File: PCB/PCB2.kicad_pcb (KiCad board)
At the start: 2 copper layers, 19.2 x 13.5 mm, 8 parts, among them J1 USB_C_Receptacle_PowerOnly_6P, Q1 T2N7002AK

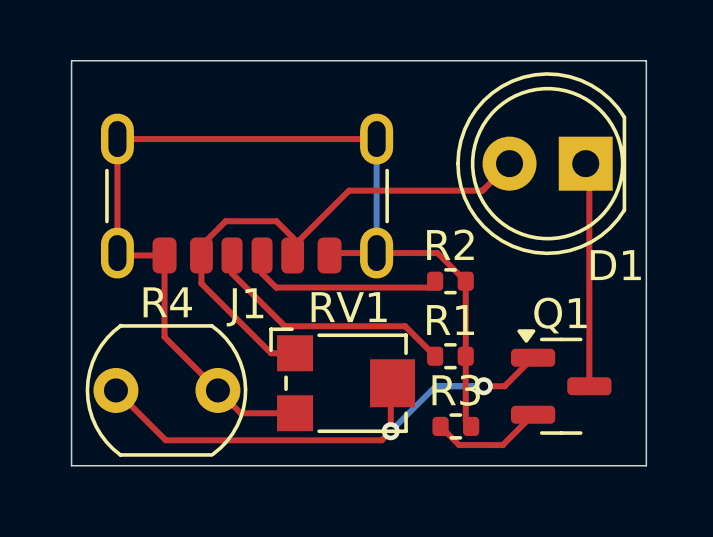
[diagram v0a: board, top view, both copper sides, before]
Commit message: Move LED to back of PCB
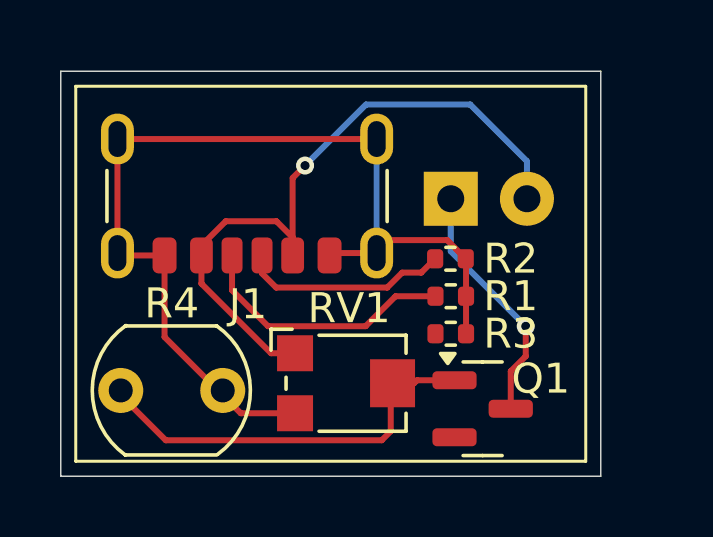
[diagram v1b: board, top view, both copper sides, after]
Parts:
- D1: moved to B.Cu
- moved D1 4.65 mm to (154.5, 93.2), turned to 0 degrees
- moved R3 3.09 mm to (154.5, 97.8)
- moved Q1 2.73 mm to (155.6, 100.2)
- moved R1 2.00 mm to (154.5, 96.5)
- moved R2 0.75 mm to (154.5, 95.2)
- moved R4 0.16 mm to (143.5, 99.6)
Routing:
- net Net-(D1-A): track 18.2 -> 23.0 mm, vias 0 -> 1
- net Net-(Q1-G): track 17.4 -> 13.6 mm, vias 2 -> 0
- net Net-(Q1-S): track 3.76 -> 0.00 mm
- net Net-(J1-SHIELD): track 35.8 -> 33.7 mm
- net Net-(D1-K): track 7.47 -> 8.24 mm, vias 0 -> 1
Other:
- board size 19.2 x 13.5 mm -> 18 x 13.5 mm
- board text added: "@Malted"
- board text added: "Thing 1.0"

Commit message: Add instructions in PCB file
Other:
- board text added: "Don't remove anything in someone else's boundary - if you want to change it then add something in your own :)"
- board text added: "Draw your edge cuts and sikscreen boundaries with the grid at 0.5mm!!"
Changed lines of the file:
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@@
 		(layer "Edge.Cuts")
+	)
+	(gr_text "Draw your edge cuts and sikscreen boundaries with the grid  at 0.5mm!!"
+		(at 138 81.5 0)
+		(layer "F.SilkS")
+		(effects
+			(font
+				(size 1 0.5)
+				(thickness 0.1)
+			)
+			(justify left bottom)
+		)
+	)
+	(gr_text "Don't remove anything in someone else's boundary -\nif you want to change it then add something in your own :)"
+		(at 152 85.5 0)
+		(layer "F.SilkS")
+		(effects
+			(font
+				(size 1 0.5)
+				(thickness 0.1)
+			)
+			(justify bottom)
+		)
 	)
 	(gr_text "Thing 1.0"

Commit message: Add the current thing to the readme
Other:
- board text added: "Don't remove anything in someone else's boundary - just add stuff in your own boundary :)"
- board text added: "Draw a rectangle around all your stuff (front and back silkscreen) and add your Slack username! :P"
- board text removed: "Don't remove anything in someone else's boundary - if you want to change it then add something in your own :)"
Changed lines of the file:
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@@
 		(layer "Edge.Cuts")
 	)
-	(gr_text "Draw your edge cuts and sikscreen boundaries with the grid  at 0.5mm!!"
-		(at 138 81.5 0)
-		(layer "F.SilkS")
-		(effects
-			(font
-				(size 1 0.5)
-				(thickness 0.1)
-			)
-			(justify left bottom)
-		)
-	)
-	(gr_text "Don't remove anything in someone else's boundary -\nif you want to change it then add something in your own :)"
+	(gr_text "Don't remove anything in someone else's boundary -\njust add stuff in your own boundary :)"
 		(at 152 85.5 0)
 		(layer "F.SilkS")
@@
 		)
 	)
+	(gr_text "Draw a rectangle around all your stuff\n(front and back silkscreen)\nand add your Slack username! :P"
+		(at 151.5 79 0)
+		(layer "F.SilkS")
+		(effects
+			(font
+				(size 1 0.5)
+				(thickness 0.1)
+			)
+			(justify bottom)
+		)
+	)
+	(gr_text "Draw your edge cuts and sikscreen boundaries with the grid  at 0.5mm!!"
+		(at 138 81.5 0)
+		(layer "B.SilkS")
+		(effects
+			(font
+				(size 1 0.5)
+				(thickness 0.1)
+			)
+			(justify left bottom)
+		)
+	)

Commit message: add my project files
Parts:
- added BZ1: Buzzer, Buzzer_Beeper:Buzzer_12x9.5RM7.6, F.Cu at (117.9, 95.6)
- added D18: D, ScottoKeebs_Components:Diode_SOD-123, B.Cu at (179.2, 101.1)
- added D3: D, ScottoKeebs_Components:Diode_SOD-123, B.Cu at (121.9, 120.6)
- added D4: D, ScottoKeebs_Components:Diode_SOD-123, B.Cu at (140.7, 120.6)
- added D5: D, ScottoKeebs_Components:Diode_SOD-123, B.Cu at (159.7, 120.6)
- added D6: D, ScottoKeebs_Components:Diode_SOD-123, B.Cu at (178.6, 120.6)
- added J2: OLED_128x64, ScottoKeebs_Components:OLED_128x32, F.Cu at (132.4, 90.1)
- added SW1: RotaryEncoder_Switch, ScottoKeebs_Components:RollerEncoder_Panasonic_EVQWGD001, F.Cu at (179.2, 95.1)
- added SW3: SW_Push_45deg, MX_Solderable:MX-Solderable-1U, F.Cu at (121.7, 114.7)
- added SW4: SW_Push_45deg, MX_Solderable:MX-Solderable-1U, F.Cu at (140.8, 114.7)
- added SW5: SW_Push_45deg, MX_Solderable:MX-Solderable-1U, F.Cu at (159.8, 114.7)
- added SW6: SW_Push_45deg, MX_Solderable:MX-Solderable-1U, F.Cu at (178.9, 114.7)
- added U2: XIAO-RP2040-DIP, Seeed Studio XIAO Series Library:XIAO-RP2040-DIP, F.Cu at (152.7, 96.9)
- moved D1 50.8 mm to (103.8, 90.4)
- moved J1 50.8 mm to (97.0, 89.2)
- moved Q1 50.8 mm to (104.8, 97.4)
- moved R1 50.8 mm to (103.8, 93.6)
- moved R2 50.8 mm to (103.8, 92.4)
- moved R3 50.8 mm to (103.8, 94.9)
- moved R4 50.8 mm to (92.8, 96.7)
- moved RV1 50.8 mm to (100.4, 96.5)
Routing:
- net /Row 0: track 0.00 -> 119.1 mm
- net GND: track 0.00 -> 90.4 mm
- net /Column 0: track 0.00 -> 48.7 mm
- net /Column 3: track 0.00 -> 41.8 mm
- net /Column 4: track 0.00 -> 40.4 mm
- net +5V: track 0.00 -> 35.4 mm
- net /ENCODER A: track 0.00 -> 33.8 mm
- net /ENCODER B: track 0.00 -> 32.0 mm
- net /BUZZER PASSIVE: track 0.00 -> 29.8 mm
- net /Column 1: track 0.00 -> 28.6 mm
- net /SCL: track 0.00 -> 14.1 mm
- net /SDA: track 0.00 -> 14.1 mm
- net Net-(D18-A): track 0.00 -> 13.6 mm
- net Net-(D6-A): track 0.00 -> 12.9 mm
- net Net-(D5-A): track 0.00 -> 12.8 mm
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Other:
- board size 18 x 13.5 mm -> 101.3 x 39.7 mm
- board text added: "@Lukas"
